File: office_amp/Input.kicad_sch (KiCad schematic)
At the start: 20 parts, among them J2 Conn_01x03_Female, J8 Conn_01x03_Female, K1 EC2-24NU, K2 EC2-24NU, K3 EC2-24NU, K4 EC2-24NU, U5 MH-M18

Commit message: Changed Components to available parts
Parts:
- removed D2, D3: WE 82350120101, Diode_SMD:D_0805_2012Metric_Pad1.15x1.40mm_HandSolder, symbol Device:D_TVS
- removed J?: Conn_01x02, symbol Connector_Generic:Conn_01x02
- removed Q? (x2): BC337, Package_TO_SOT_THT:TO-92_Inline, symbol Transistor_BJT:BC337
- added D2, D3: WE 824500700, Diode_SMD:D_SMA_Handsoldering, symbol LagerVerwaltung:D_TVS_UNI
- added Q4, Q5: BC850, Package_TO_SOT_SMD:SOT-23, symbol Transistor_BJT:BC850
- added STAR5: SolderJumper_2_Bridged, Jumper:SolderJumper-2_P1.3mm_Bridged_RoundedPad1.0x1.5mm, symbol Jumper:SolderJumper_2_Bridged
- R15, R16, R17, R18: renamed from R?; footprint (none) -> Resistor_SMD:R_0805_2012Metric_Pad1.20x1.40mm_HandSolder
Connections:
- net GND2: now also Q4.2 (E), Q5.2 (E), STAR5.1 (A)
- net GND_An_In: now also D2.2 (A), D3.2 (A)
- net L-In-An: now also D3.1 (K)
- net R-In-An: now also D2.1 (K)
- net at D1.2 (A), K1.12: now also D4.2 (A), K2.12, Q4.3 (C)
- net at D6.2 (A), K4.12: now also D5.2 (A), K3.12, Q5.3 (C)
- net SELECT-Analog: now reaches R15.1
- net at R17.2, R18.2: now also Q5.1 (B)
- net at R15.2, R16.2: now also Q4.1 (B)
- net SELECT-BT: now reaches R17.1
- new net GNDREF: STAR5.2 (B)
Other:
- note removed: "NEU 824500700!!!!!!!"
- moved on the sheet: D1, D4, D5, D6, K1, K2, K3, K4, R15, R16, R17, R18

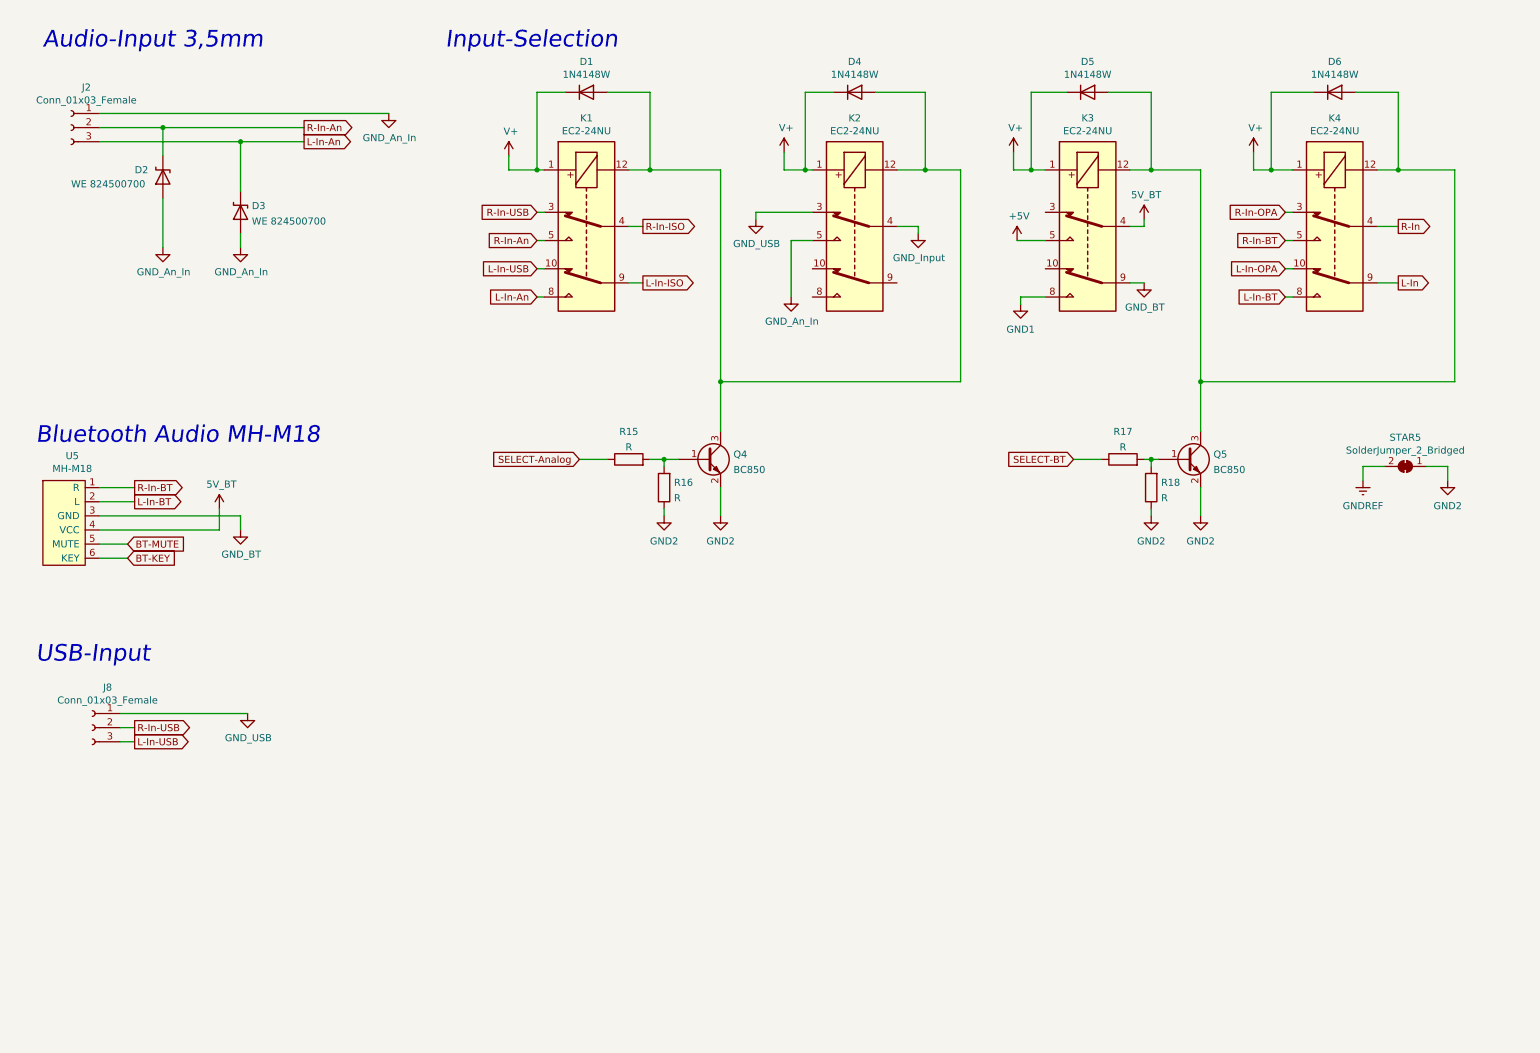
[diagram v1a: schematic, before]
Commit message: First positioning of new components (top site), added mounting holes for case  compabillity (Donau 523178)
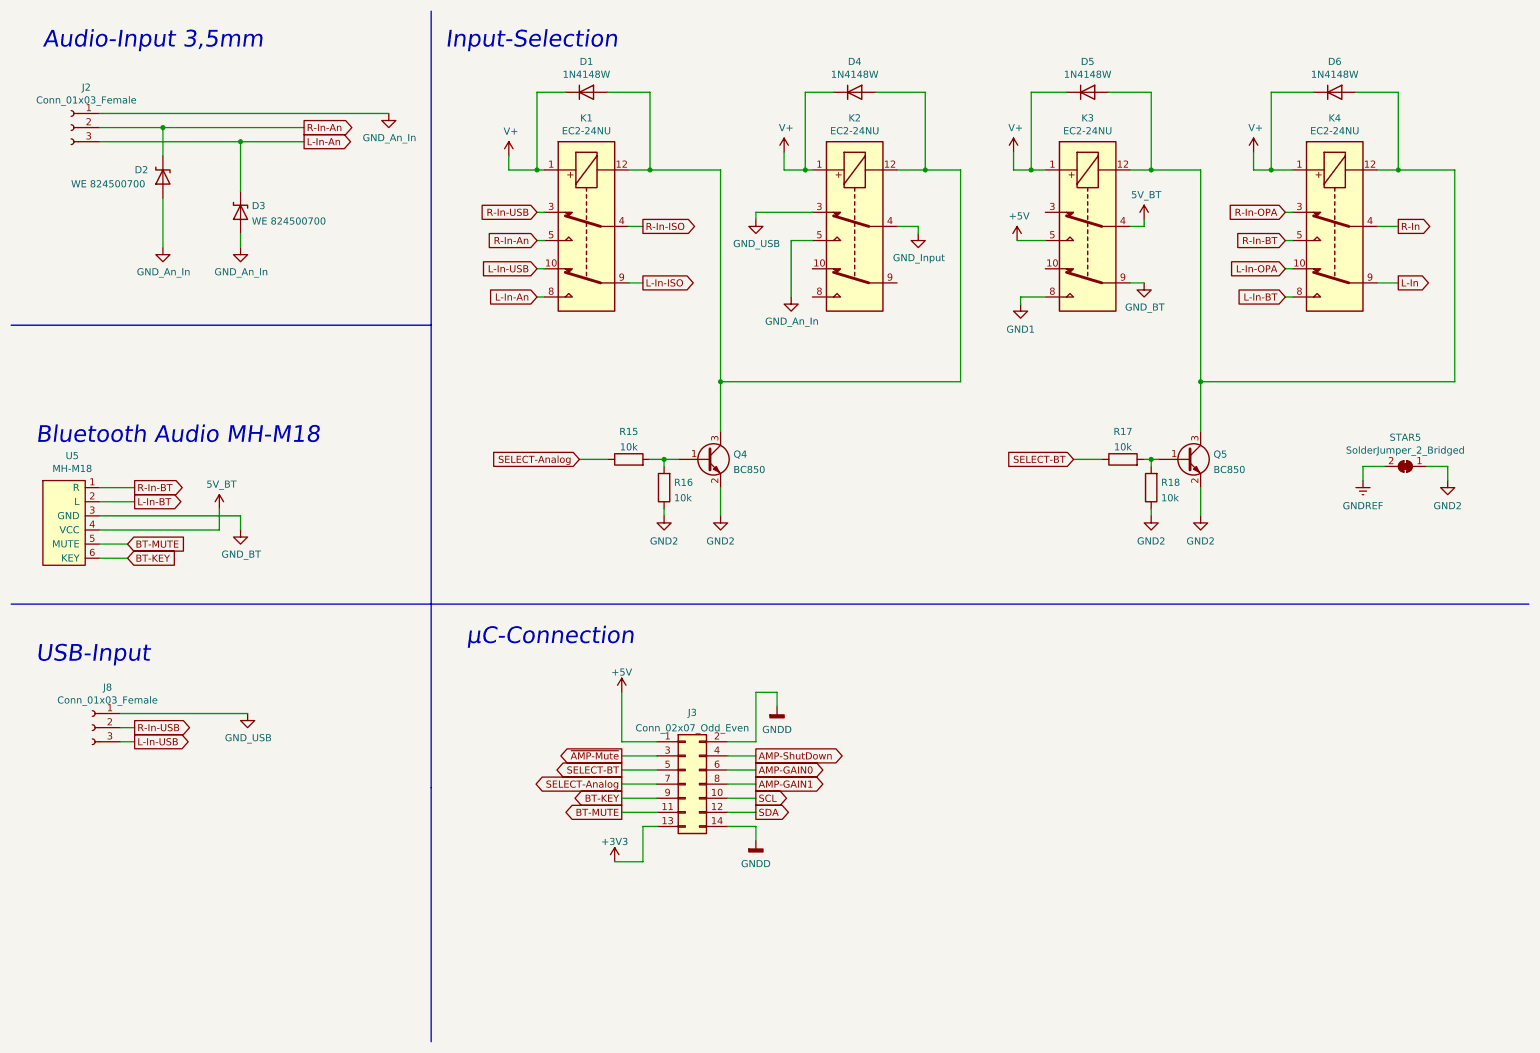
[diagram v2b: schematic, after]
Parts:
- added J3: Conn_02x07_Odd_Even, Connector_IDC:IDC-Header_2x07_P2.54mm_Vertical, symbol Connector_Generic:Conn_02x07_Odd_Even
- R15, R16, R17, R18: value R -> 10k
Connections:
- net +5V: now also J3.1 (Pin_1)
- net BT-KEY: now also J3.9 (Pin_9)
- net BT-MUTE: now also J3.11 (Pin_11)
- net SELECT-Analog: now also J3.7 (Pin_7)
- net SELECT-BT: now also J3.5 (Pin_5)
- new net +3V3: J3.13 (Pin_13)
- new net AMP-GAIN0: J3.6 (Pin_6)
- new net AMP-GAIN1: J3.8 (Pin_8)
- new net AMP-ShutDown: J3.4 (Pin_4)
- new net GNDD: J3.14 (Pin_14), J3.2 (Pin_2)
- new net SCL: J3.10 (Pin_10)
- new net SDA: J3.12 (Pin_12)
- new net ~{AMP-Mute}: J3.3 (Pin_3)
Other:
- note added: "µC-Connection"

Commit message: Completed PCB-Layout V1
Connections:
- net GND_BT: no longer J8.1 (Pin_1), K2.3
- net SCL: now also J3.12 (Pin_12); no longer J3.10 (Pin_10)
- net SDA: now also J3.10 (Pin_10); no longer J3.12 (Pin_12)
- new net GND_USB: J8.1 (Pin_1), K2.3
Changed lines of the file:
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@@
+    (stroke (width 0) (type default) (color 0 0 0 0))
+  )
+  (wire (pts (xy 53.34 138.43) (xy 53.34 140.97))
     (stroke (width 0) (type default) (color 0 0 0 0))
   )
@@
     (stroke (width 0) (type default) (color 0 0 0 0))
   )
+  (wire (pts (xy 140.97 153.67) (xy 146.05 153.67))
+    (stroke (width 0) (type default) (color 0 0 0 0))
+  )
   (wire (pts (xy 152.4 63.5) (xy 152.4 53.34))
     (stroke (width 0) (type default) (color 0 0 0 0))
@@
     (stroke (width 0) (type default) (color 0 0 0 0))
   )
-  (wire (pts (xy 140.97 153.67) (xy 146.05 153.67))
-    (stroke (width 0) (type default) (color 0 0 0 0))
-  )
   (wire (pts (xy 27.94 107.95) (xy 33.02 107.95))
     (stroke (width 0) (type default) (color 0 0 0 0))
@@
     (stroke (width 0) (type default) (color 0 0 0 0))
   )
-  (wire (pts (xy 31.75 138.43) (xy 54.61 138.43))
-    (stroke (width 0) (type default) (color 0 0 0 0))
-  )
   (wire (pts (xy 106.68 26.67) (xy 106.68 40.64))
     (stroke (width 0) (type default) (color 0 0 0 0))
@@
     (stroke (width 0) (type default) (color 0 0 0 0))
   )
+  (wire (pts (xy 146.05 48.26) (xy 156.21 48.26))
+    (stroke (width 0) (type default) (color 0 0 0 0))
+  )
   (wire (pts (xy 217.17 40.64) (xy 217.17 26.67))
     (stroke (width 0) (type default) (color 0 0 0 0))
@@
     (stroke (width 0) (type default) (color 0 0 0 0))
   )
+  (wire (pts (xy 140.97 156.21) (xy 146.05 156.21))
+    (stroke (width 0) (type default) (color 0 0 0 0))
+  )
   (wire (pts (xy 27.94 105.41) (xy 49.53 105.41))
     (stroke (width 0) (type default) (color 0 0 0 0))
@@
     (stroke (width 0) (type default) (color 0 0 0 0))
   )
-  (wire (pts (xy 146.05 49.53) (xy 146.05 48.26))
-    (stroke (width 0) (type default) (color 0 0 0 0))
-  )
   (wire (pts (xy 217.17 40.64) (xy 226.06 40.64))
     (stroke (width 0) (type default) (color 0 0 0 0))
@@
     (stroke (width 0) (type default) (color 0 0 0 0))
   )
-  (wire (pts (xy 146.05 48.26) (xy 156.21 48.26))
-    (stroke (width 0) (type default) (color 0 0 0 0))
-  )
   (wire (pts (xy 127 92.71) (xy 129.54 92.71))
     (stroke (width 0) (type default) (color 0 0 0 0))
@@
     (stroke (width 0) (type default) (color 0 0 0 0))
   )
+  (wire (pts (xy 31.75 138.43) (xy 53.34 138.43))
+    (stroke (width 0) (type default) (color 0 0 0 0))
+  )
   (wire (pts (xy 121.92 146.05) (xy 128.27 146.05))
     (stroke (width 0) (type default) (color 0 0 0 0))
   )
-  (wire (pts (xy 140.97 156.21) (xy 146.05 156.21))
+  (wire (pts (xy 146.05 50.8) (xy 146.05 48.26))
     (stroke (width 0) (type default) (color 0 0 0 0))
   )
@@
     )
   )
-  (global_label "SCL" (shape output) (at 146.05 153.67 0) (fields_autoplaced)
-    (effects (font (size 1.27 1.27)) (justify left))
-    (property "Intersheet References" "${INTERSHEET_REFS}" (id 0) (at 151.8818 153.5906 0)
+  (global_label "SCL" (shape output) (at 146.05 156.21 0) (fields_autoplaced)
+    (effects (font (size 1.27 1.27)) (justify left))
+    (property "Intersheet References" "${INTERSHEET_REFS}" (id 0) (at 151.8818 156.1306 0)
       (effects (font (size 1.27 1.27)) (justify left) hide)
     )
@@
     )
   )
-  (global_label "SDA" (shape output) (at 146.05 156.21 0) (fields_autoplaced)
-    (effects (font (size 1.27 1.27)) (justify left))
-    (property "Intersheet References" "${INTERSHEET_REFS}" (id 0) (at 151.9423 156.1306 0)
+  (global_label "SDA" (shape output) (at 146.05 153.67 0) (fields_autoplaced)
+    (effects (font (size 1.27 1.27)) (justify left))
+    (property "Intersheet References" "${INTERSHEET_REFS}" (id 0) (at 151.9423 153.5906 0)
       (effects (font (size 1.27 1.27)) (justify left) hide)
     )
@@
     (pin "9")
   )
-  (symbol (lib_id "OfficeAmp:GND_USB") (at 146.05 49.53 0) (unit 1)
-    (in_bom yes) (on_board yes)
-    (property "Reference" "#PWR021" (id 0) (at 146.05 55.88 0)
-      (effects (font (size 1.27 1.27)) hide)
-    )
-    (property "Value" "GND_USB" (id 1) (at 146.177 53.9242 0))
-    (property "Footprint" "" (id 2) (at 146.05 49.53 0)
-      (effects (font (size 1.27 1.27)) hide)
-    )
-    (property "Datasheet" "" (id 3) (at 146.05 49.53 0)
-      (effects (font (size 1.27 1.27)) hide)
-    )
-    (pin "1")
-  )
   (symbol (lib_id "OfficeAmp:GND_Input") (at 175.26 52.07 0) (unit 1)
     (in_bom yes) (on_board yes)
@@
     (pin "2")
     (pin "3")
-  )
-  (symbol (lib_id "OfficeAmp:GND_USB") (at 54.61 138.43 0) (unit 1)
-    (in_bom yes) (on_board yes)
-    (property "Reference" "#PWR020" (id 0) (at 54.61 144.78 0)
-      (effects (font (size 1.27 1.27)) hide)
-    )
-    (property "Value" "GND_USB" (id 1) (at 54.737 142.8242 0))
-    (property "Footprint" "" (id 2) (at 54.61 138.43 0)
-      (effects (font (size 1.27 1.27)) hide)
-    )
-    (property "Datasheet" "" (id 3) (at 54.61 138.43 0)
-      (effects (font (size 1.27 1.27)) hide)
-    )
-    (pin "1")
   )
   (symbol (lib_id "OfficeAmp:GND_An_In") (at 80.01 30.48 0) (unit 1)
@@
     (pin "9")
   )
+  (symbol (lib_id "OfficeAmp:GND_USB") (at 146.05 50.8 0) (unit 1)
+    (in_bom yes) (on_board yes) (fields_autoplaced)
+    (property "Reference" "#PWR?" (id 0) (at 146.05 57.15 0)
+      (effects (font (size 1.27 1.27)) hide)
+    )
+    (property "Value" "GND_USB" (id 1) (at 146.05 55.3625 0))
+    (property "Footprint" "" (id 2) (at 146.05 50.8 0)
+      (effects (font (size 1.27 1.27)) hide)
+    )
+    (property "Datasheet" "" (id 3) (at 146.05 50.8 0)
+      (effects (font (size 1.27 1.27)) hide)
+    )
+    (pin "1")
+  )
   (symbol (lib_id "power:GND1") (at 193.675 64.77 0) (unit 1)
     (in_bom yes) (on_board yes) (fields_autoplaced)
@@
     (pin "2")
   )
+  (symbol (lib_id "OfficeAmp:GND_USB") (at 53.34 140.97 0) (unit 1)
+    (in_bom yes) (on_board yes) (fields_autoplaced)
+    (property "Reference" "#PWR?" (id 0) (at 53.34 147.32 0)
+      (effects (font (size 1.27 1.27)) hide)
+    )
+    (property "Value" "GND_USB" (id 1) (at 53.34 145.5325 0))
+    (property "Footprint" "" (id 2) (at 53.34 140.97 0)
+      (effects (font (size 1.27 1.27)) hide)
+    )
+    (property "Datasheet" "" (id 3) (at 53.34 140.97 0)
+      (effects (font (size 1.27 1.27)) hide)
+    )
+    (pin "1")
+  )
   (symbol (lib_id "Jumper:SolderJumper_2_Bridged") (at 262.89 93.98 0) (mirror y) (unit 1)

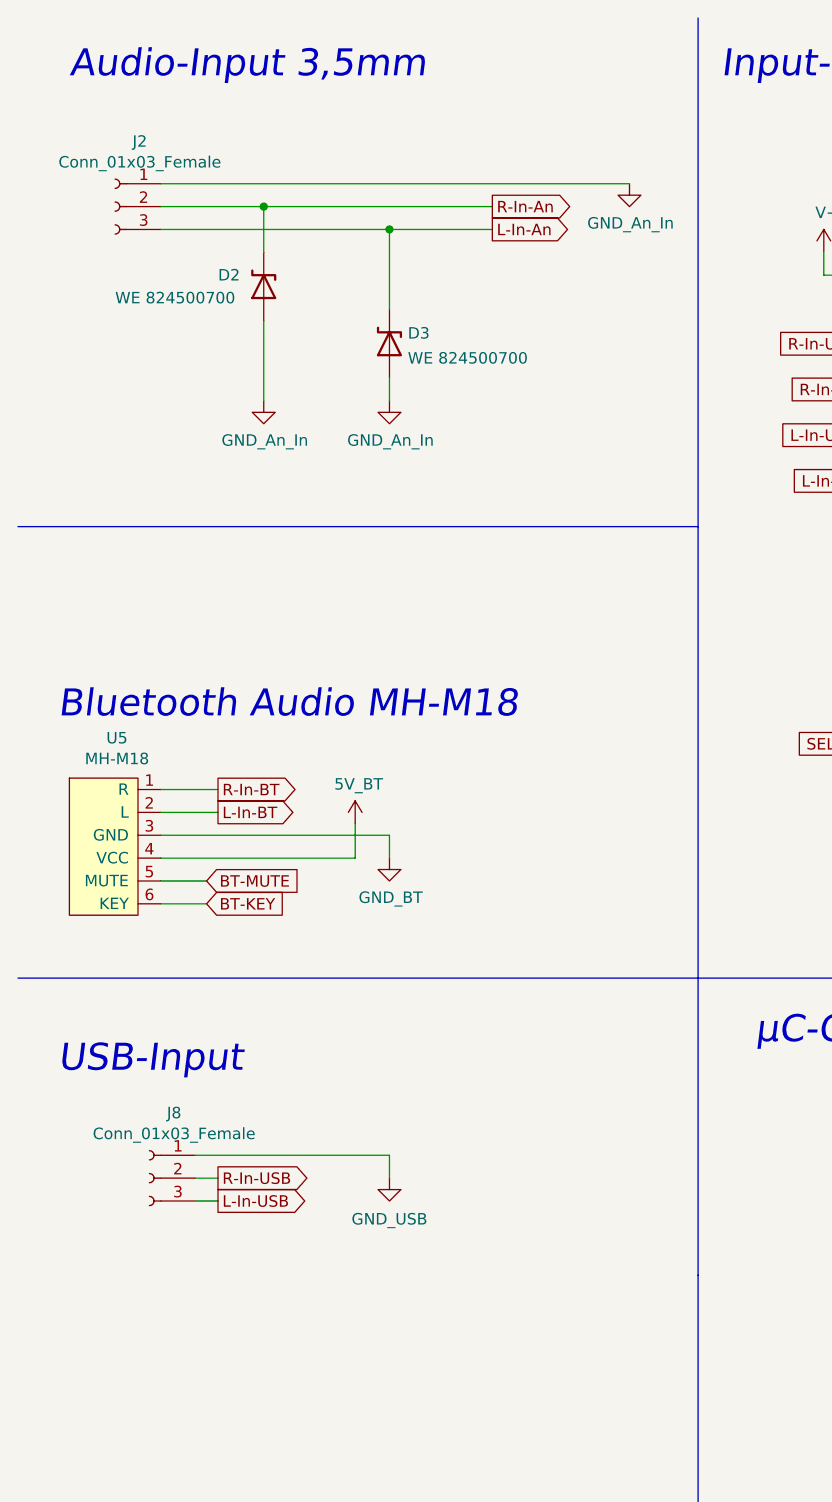
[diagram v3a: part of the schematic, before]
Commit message: added testpoints, corrected footprints, removed ground loop dgnd gnda
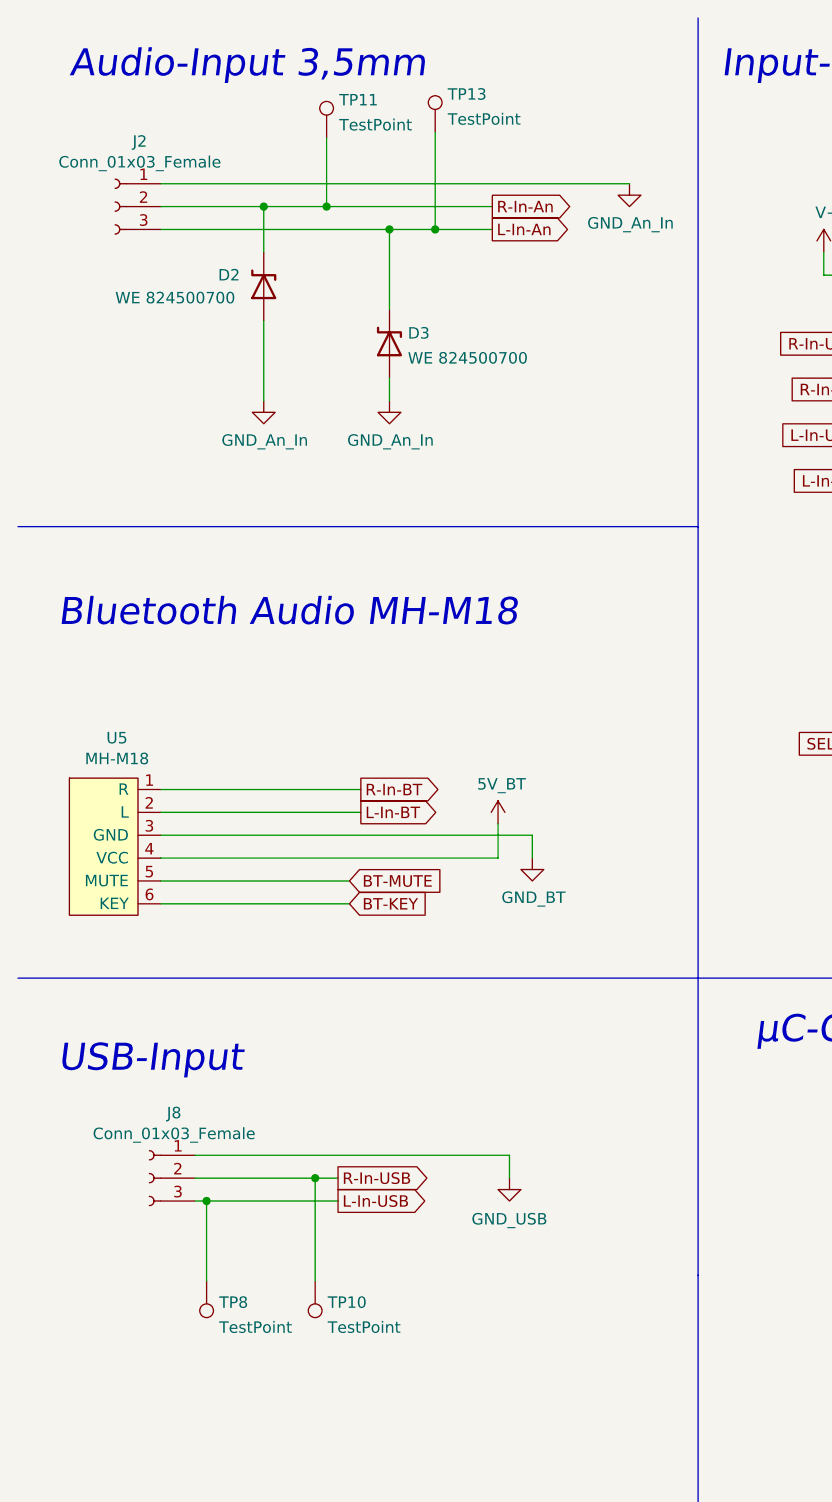
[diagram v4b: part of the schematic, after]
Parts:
- added TP10, TP11, TP13, TP8: TestPoint, TestPoint:TestPoint_Pad_D1.0mm, symbol Connector:TestPoint
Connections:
- net L-In-An: now also TP13.1
- net L-In-USB: now also TP8.1
- net R-In-An: now also TP11.1
- net R-In-USB: now also TP10.1
